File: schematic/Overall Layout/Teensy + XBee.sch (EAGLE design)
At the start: 15 parts, among them U4 MAX13054ASA

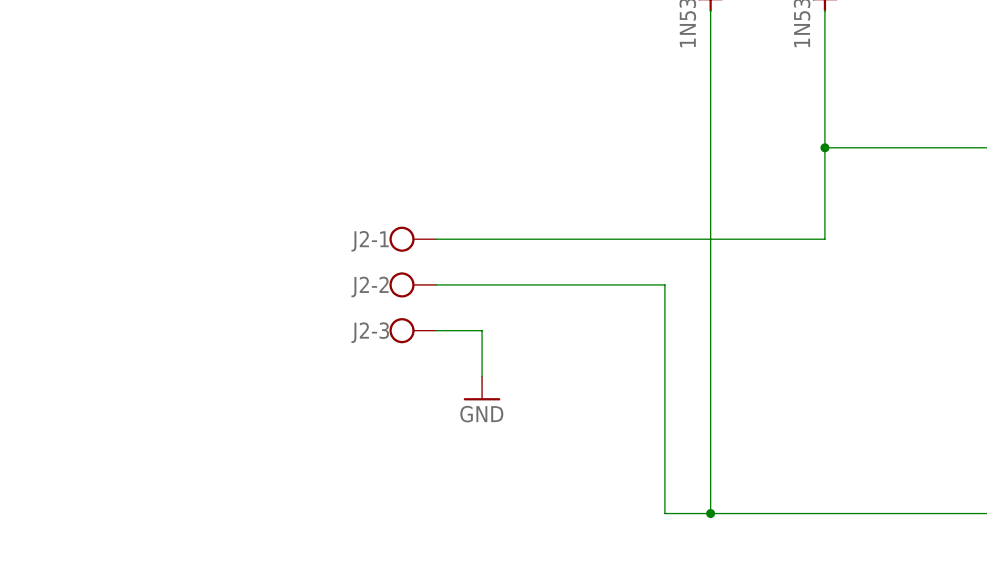
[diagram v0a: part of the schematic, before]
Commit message: Added military connectors to CAN Bus and added copper threading to PCB designs
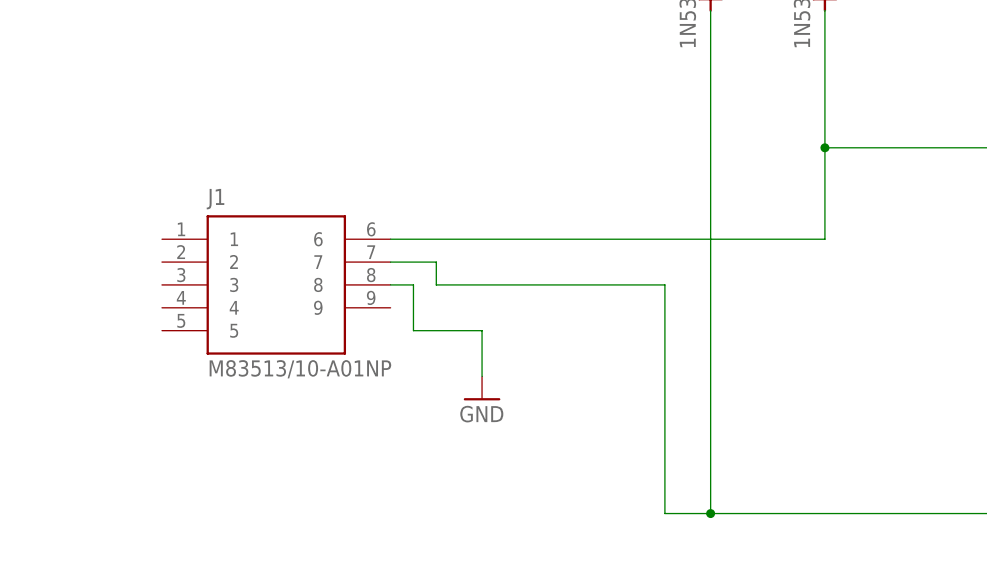
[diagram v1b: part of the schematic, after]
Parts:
- removed J2: (no value), con-wago-500:W237-103
- added J1: M83513/10-A01NP, M83513_10-A01NP:M83513/10-A01NP
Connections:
- net CAN_BUS: now also J1.6; no longer J2-1.KL
- net GND: now also J1.8; no longer J2-3.KL
- net N$3: now also J1.7; no longer J2-2.KL
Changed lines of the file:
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@@
 </variantdefs>
 <classes>
-<class number="0" name="default" width="0" drill="0">
+<class number="0" name="default" width="0.3048" drill="0.508">
+<clearance class="0" value="0.254"/>
 </class>
 </classes>
@@
 <part name="D8" library="diode" library_urn="urn:adsk.eagle:library:210" deviceset="1N5333" device="" package3d_urn="urn:adsk.eagle:package:43351/1"/>
 <part name="D9" library="diode" library_urn="urn:adsk.eagle:library:210" deviceset="1N5333" device="" package3d_urn="urn:adsk.eagle:package:43351/1"/>
-<part name="J2" library="con-wago-500" library_urn="urn:adsk.eagle:library:195" deviceset="W237-103" device="" package3d_urn="urn:adsk.eagle:package:10691/1"/>
 <part name="GND15" library="supply1" library_urn="urn:adsk.eagle:library:371" deviceset="GND" device=""/>
 <part name="GND16" library="supply1" library_urn="urn:adsk.eagle:library:371" deviceset="GND" device=""/>
@@
 <part name="S15" library="switch-tact" deviceset="DTS-6" device=""/>
 <part name="XB2" library="maxstream" library_urn="urn:adsk.eagle:library:270" deviceset="XBEE" device="" package3d_urn="urn:adsk.eagle:package:18007/1"/>
+<part name="J1" library="M83513_10-A01NP" deviceset="M83513/10-A01NP" device=""/>
 </parts>
 <sheets>
@@
 <attribute name="VALUE" x="46.609" y="135.382" size="1.778" layer="96" rot="R90"/>
 </instance>
-<instance part="J2" gate="-1" x="-5.08" y="99.06" smashed="yes">
-<attribute name="NAME" x="-5.08" y="99.949" size="1.778" layer="95" rot="R180"/>
-</instance>
-<instance part="J2" gate="-2" x="-5.08" y="93.98" smashed="yes">
-<attribute name="NAME" x="-5.08" y="94.869" size="1.778" layer="95" rot="R180"/>
-</instance>
-<instance part="J2" gate="-3" x="-5.08" y="88.9" smashed="yes">
-<attribute name="VALUE" x="-7.62" y="85.217" size="1.778" layer="96"/>
-<attribute name="NAME" x="-5.08" y="89.789" size="1.778" layer="95" rot="R180"/>
-</instance>
 <instance part="GND15" gate="1" x="38.1" y="147.32" smashed="yes" rot="R180">
 <attribute name="VALUE" x="40.64" y="149.86" size="1.778" layer="96" rot="R180"/>
@@
 <attribute name="NAME" x="-73.66" y="8.89" size="1.778" layer="95" rot="R180"/>
 <attribute name="VALUE" x="-73.66" y="71.12" size="1.778" layer="96" rot="R180"/>
+</instance>
+<instance part="J1" gate="G$1" x="-17.78" y="93.98" smashed="yes">
+<attribute name="NAME" x="-25.4" y="102.87" size="1.778" layer="95"/>
+<attribute name="VALUE" x="-25.4" y="83.82" size="1.778" layer="96"/>
 </instance>
 </instances>
@@
 </segment>
 <segment>
-<pinref part="J2" gate="-3" pin="KL"/>
-<wire x1="0" y1="88.9" x2="5.08" y2="88.9" width="0.1524" layer="91"/>
+<wire x1="-2.54" y1="88.9" x2="5.08" y2="88.9" width="0.1524" layer="91"/>
 <pinref part="GND16" gate="1" pin="GND"/>
 <wire x1="5.08" y1="88.9" x2="5.08" y2="83.82" width="0.1524" layer="91"/>
+<wire x1="-2.54" y1="88.9" x2="-2.54" y2="93.98" width="0.1524" layer="91"/>
+<pinref part="J1" gate="G$1" pin="8"/>
+<wire x1="-2.54" y1="93.98" x2="-5.08" y2="93.98" width="0.1524" layer="91"/>
 </segment>
 <segment>
@@
 <wire x1="30.48" y1="124.46" x2="30.48" y2="68.58" width="0.1524" layer="91"/>
 <wire x1="30.48" y1="68.58" x2="66.04" y2="68.58" width="0.1524" layer="91"/>
-<pinref part="J2" gate="-2" pin="KL"/>
 <wire x1="0" y1="93.98" x2="25.4" y2="93.98" width="0.1524" layer="91"/>
 <wire x1="25.4" y1="93.98" x2="25.4" y2="68.58" width="0.1524" layer="91"/>
 <wire x1="25.4" y1="68.58" x2="30.48" y2="68.58" width="0.1524" layer="91"/>
 <junction x="30.48" y="68.58"/>
+<wire x1="0" y1="93.98" x2="0" y2="96.52" width="0.1524" layer="91"/>
+<pinref part="J1" gate="G$1" pin="7"/>
+<wire x1="0" y1="96.52" x2="-5.08" y2="96.52" width="0.1524" layer="91"/>
 </segment>
 </net>
@@
 <wire x1="43.18" y1="124.46" x2="43.18" y2="109.22" width="0.1524" layer="91"/>
 <wire x1="43.18" y1="109.22" x2="66.04" y2="109.22" width="0.1524" layer="91"/>
-<pinref part="J2" gate="-1" pin="KL"/>
-<wire x1="0" y1="99.06" x2="43.18" y2="99.06" width="0.1524" layer="91"/>
+<wire x1="-5.08" y1="99.06" x2="43.18" y2="99.06" width="0.1524" layer="91"/>
 <wire x1="43.18" y1="99.06" x2="43.18" y2="109.22" width="0.1524" layer="91"/>
 <junction x="43.18" y="109.22"/>
+<pinref part="J1" gate="G$1" pin="6"/>
 </segment>
 </net>
